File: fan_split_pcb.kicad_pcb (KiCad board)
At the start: 2 copper layers, 23 x 14.5 mm, 4 parts

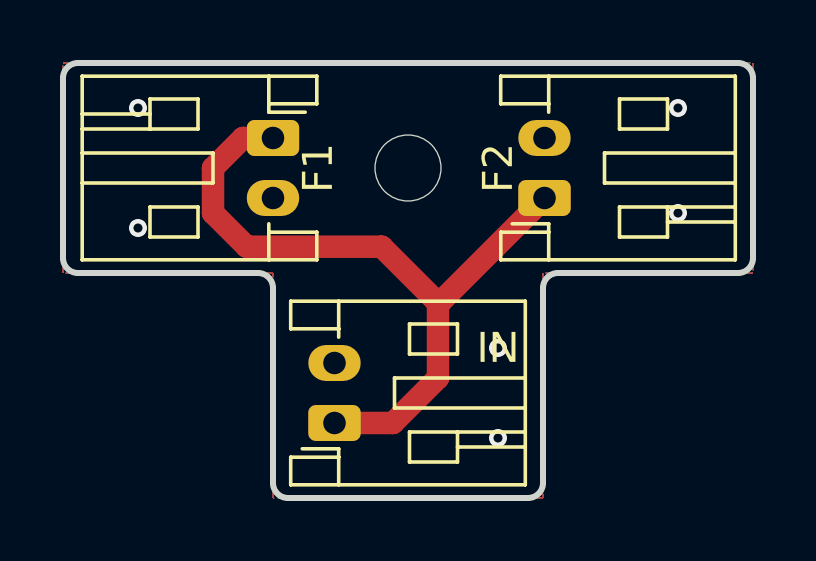
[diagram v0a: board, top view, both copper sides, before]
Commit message: modified m2 mounting hole and added production files
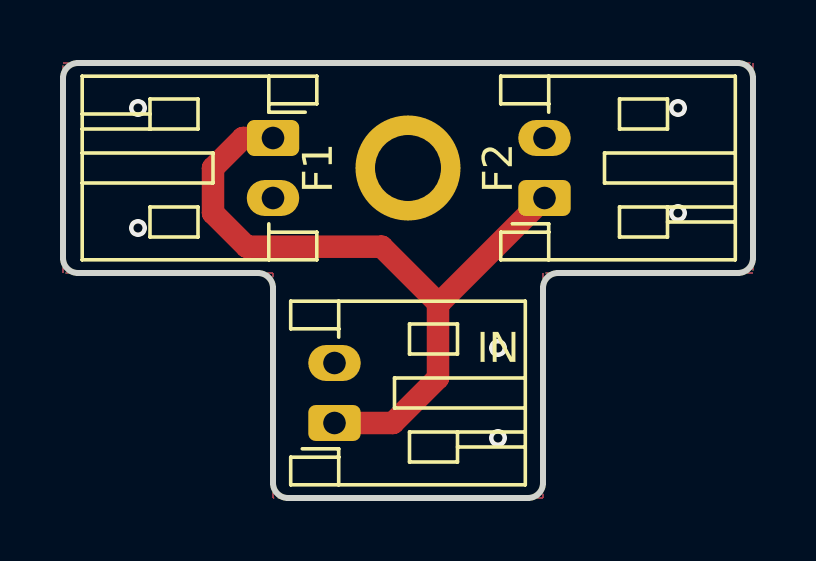
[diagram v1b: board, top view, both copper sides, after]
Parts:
- REF**: value MountingHole_2.2mm_M2_DIN965 -> MountingHole_2.2mm_M2_ISO7380_Pad; footprint MountingHole:MountingHole_2.2mm_M2_DIN965 -> MountingHole:MountingHole_2.2mm_M2_ISO7380_Pad
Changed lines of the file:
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@@
 	(net 1 "VDD")
 	(net 2 "GND")
-	(footprint "MountingHole:MountingHole_2.2mm_M2_DIN965"
+	(footprint "MountingHole:MountingHole_2.2mm_M2_ISO7380_Pad"
 		(layer "F.Cu")
 		(at 56 47)
-		(descr "Mounting Hole 2.2mm, no annular, M2, DIN965")
-		(tags "mounting hole 2.2mm no annular m2 din965")
+		(descr "Mounting Hole 2.2mm, M2, ISO7380")
+		(tags "mounting hole 2.2mm m2 iso7380")
 		(property "Reference" "REF**"
-			(at 0 -2.9 0)
+			(at 0 -2.75 0)
 			(layer "F.SilkS")
 			(hide yes)
@@
 			)
 		)
-		(property "Value" "MountingHole_2.2mm_M2_DIN965"
-			(at 0 2.9 0)
+		(property "Value" "MountingHole_2.2mm_M2_ISO7380_Pad"
+			(at 0 2.75 0)
 			(layer "F.Fab")
 			(effects
@@
 		(fp_circle
 			(center 0 0)
-			(end 1.9 0)
+			(end 1.75 0)
 			(stroke
 				(width 0.15)
@@
 		(fp_circle
 			(center 0 0)
-			(end 2.15 0)
+			(end 2 0)
 			(stroke
 				(width 0.05)
@@
 			)
 		)
-		(pad "" np_thru_hole circle
+		(pad "1" thru_hole circle
 			(at 0 0)
-			(size 2.2 2.2)
+			(size 3.5 3.5)
 			(drill 2.2)
 			(layers "*.Cu" "*.Mask")
+			(remove_unused_layers no)
 		)
 		(embedded_fonts no)
